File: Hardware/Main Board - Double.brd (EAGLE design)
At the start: 124.5 x 73.7 mm, 104 parts, among them J1 MICROMOD-2222-C, J10 MICRO-SD-PUSH-PUSH-EXT-PIN, J2 Vertical Qwiic Connector, J4 QWIIC_RIGHT_ANGLE, J5 CORTEX_JTAG_DEBUG_MINIMUM_PTH, J6 MICROMOD_CARRIER, J7 MICROMOD_CARRIER, Q1 3.1A/30V/105mΩ, U2 MCP73831, U5 AP7361C-33

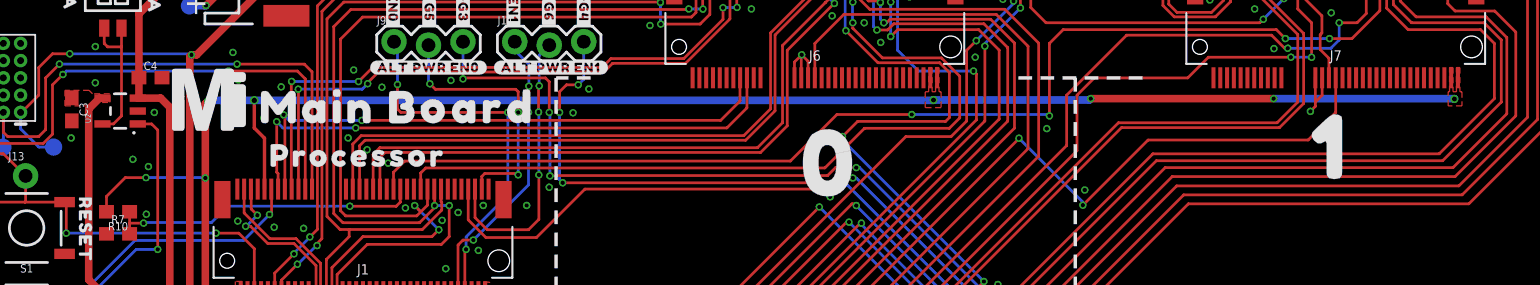
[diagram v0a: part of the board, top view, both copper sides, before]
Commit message: Changes power to Function Boards @ VCC to VCC rather than VIN
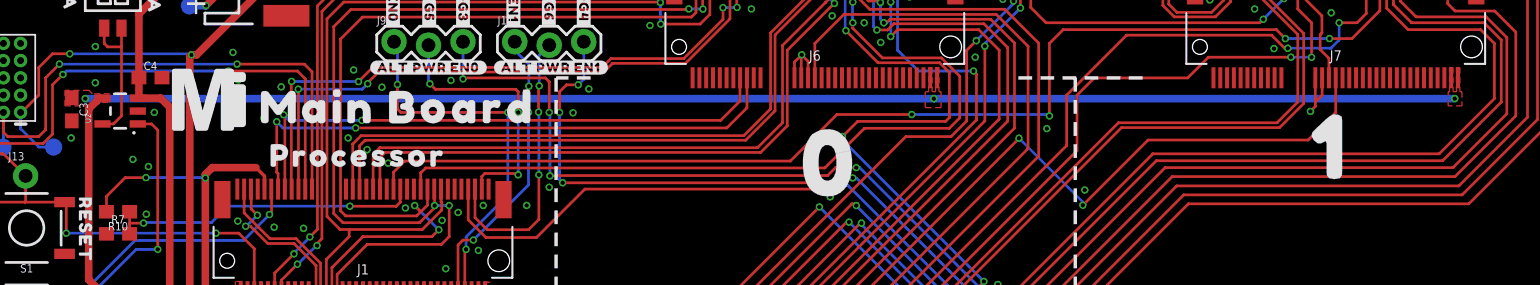
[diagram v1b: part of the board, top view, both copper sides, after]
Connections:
- net VCC: now also J6.72, J6.74, J7.72, J7.74
- net VIN: no longer J6.72, J6.74, J7.72, J7.74
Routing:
- net VCC: track 55.5 -> 156.4 mm, vias 2 -> 5
- net VIN: track 179.2 -> 80.7 mm, vias 9 -> 3
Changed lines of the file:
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@@
 <via x="37.4526" y="48.2628" extent="1-16" drill="0.3048"/>
 <via x="34.7856" y="50.4726" extent="1-16" drill="0.3048"/>
+<wire x1="21.206" y1="52.773" x2="19.706" y2="52.773" width="0" layer="19" extent="1-1"/>
+<wire x1="22.4158" y1="49.9646" x2="19.7358" y2="50.419" width="0" layer="19" extent="1-1"/>
 </signal>
 <signal name="V_BATT" class="1">
@@
 <wire x1="2.286" y1="29.972" x2="5.2324" y2="29.972" width="0.2032" layer="1"/>
 <wire x1="9.7743" y1="59.4716" x2="9.5606" y2="59.4716" width="0.5588" layer="1"/>
-<wire x1="9.5606" y1="59.4716" x2="8.763" y2="58.674" width="0.5588" layer="1"/>
+<wire x1="9.5606" y1="59.4716" x2="9.3345" y2="59.2455" width="0.5588" layer="1"/>
+<wire x1="9.3345" y1="59.2455" x2="8.763" y2="58.674" width="0.5588" layer="1"/>
 <wire x1="8.763" y1="46.101" x2="8.763" y2="58.674" width="0.5588" layer="1"/>
 <wire x1="15.113" y1="28.321" x2="14.7066" y2="27.9146" width="0.5588" layer="1"/>
@@
 <contactref element="Q1" pad="2"/>
 <contactref element="D5" pad="C"/>
+<contactref element="J6" pad="72"/>
+<contactref element="J6" pad="74"/>
+<contactref element="J7" pad="72"/>
+<contactref element="J7" pad="74"/>
+<polygon width="0.127" layer="1" thermals="no">
+<vertex x="70.612" y="61.722"/>
+<vertex x="70.866" y="61.722"/>
+<vertex x="70.866" y="59.944"/>
+<vertex x="71.12" y="59.944"/>
+<vertex x="71.12" y="61.722"/>
+<vertex x="71.374" y="61.722"/>
+<vertex x="71.374" y="59.944"/>
+<vertex x="71.5264" y="59.944"/>
+<vertex x="71.5264" y="58.7756"/>
+<vertex x="70.358" y="58.7756"/>
+<vertex x="70.358" y="59.944"/>
+<vertex x="70.612" y="59.944"/>
+</polygon>
+<polygon width="0.127" layer="1" thermals="no">
+<vertex x="108.966" y="61.722"/>
+<vertex x="109.22" y="61.722"/>
+<vertex x="109.22" y="59.944"/>
+<vertex x="109.474" y="59.944"/>
+<vertex x="109.474" y="61.722"/>
+<vertex x="109.728" y="61.722"/>
+<vertex x="109.728" y="59.944"/>
+<vertex x="109.8804" y="59.944"/>
+<vertex x="109.8804" y="58.9026"/>
+<vertex x="108.8644" y="58.9026"/>
+<vertex x="108.8644" y="59.944"/>
+<vertex x="108.966" y="59.944"/>
+</polygon>
+<via x="8.509" y="59.436" extent="1-16" drill="0.3048"/>
+<wire x1="8.509" y1="59.436" x2="70.993" y2="59.436" width="0.5588" layer="16"/>
+<via x="109.347" y="59.436" extent="1-16" drill="0.3048"/>
+<wire x1="70.993" y1="59.436" x2="109.347" y2="59.436" width="0.5588" layer="16"/>
+<via x="70.993" y="59.436" extent="1-16" drill="0.3048"/>
 </signal>
 <signal name="!CS1!-PROCESSOR">
@@
 <contactref element="R8" pad="2"/>
 <contactref element="D5" pad="A"/>
-<contactref element="J7" pad="72"/>
-<contactref element="J7" pad="74"/>
-<contactref element="J6" pad="72"/>
-<contactref element="J6" pad="74"/>
 <wire x1="13.1826" y1="15.748" x2="13.6652" y2="16.2306" width="0.5588" layer="1"/>
 <wire x1="13.6652" y1="16.2306" x2="13.6652" y2="16.9094" width="0.5588" layer="1"/>
 <wire x1="13.6652" y1="16.9094" x2="15.1314" y2="16.9094" width="0.5588" layer="1"/>
 <wire x1="15.1314" y1="16.9094" x2="17.3482" y2="19.1262" width="0.5588" layer="1"/>
-<via x="17.5514" y="59.2582" extent="1-16" drill="0.35"/>
-<wire x1="17.3482" y1="59.055" x2="17.3482" y2="53.594" width="0.5588" layer="1"/>
+<wire x1="17.3482" y1="53.594" x2="17.3482" y2="53.848" width="0.5588" layer="1"/>
 <wire x1="17.3482" y1="53.594" x2="17.3482" y2="19.1262" width="0.5588" layer="1"/>
-<wire x1="17.3482" y1="59.055" x2="17.5514" y2="59.2582" width="0.5588" layer="1"/>
-<wire x1="17.5514" y1="59.2582" x2="17.6022" y2="59.309" width="0.5588" layer="16"/>
-<polygon width="0.127" layer="1" thermals="no">
-<vertex x="108.966" y="61.722"/>
-<vertex x="109.22" y="61.722"/>
-<vertex x="109.22" y="59.944"/>
-<vertex x="109.474" y="59.944"/>
-<vertex x="109.474" y="61.722"/>
-<vertex x="109.728" y="61.722"/>
-<vertex x="109.728" y="59.944"/>
-<vertex x="109.8804" y="59.944"/>
-<vertex x="109.8804" y="58.9026"/>
-<vertex x="108.8644" y="58.9026"/>
-<vertex x="108.8644" y="59.944"/>
-<vertex x="108.966" y="59.944"/>
-</polygon>
-<polygon width="0.127" layer="1" thermals="no">
-<vertex x="70.612" y="61.722"/>
-<vertex x="70.866" y="61.722"/>
-<vertex x="70.866" y="59.944"/>
-<vertex x="71.12" y="59.944"/>
-<vertex x="71.12" y="61.722"/>
-<vertex x="71.374" y="61.722"/>
-<vertex x="71.374" y="59.944"/>
-<vertex x="71.5264" y="59.944"/>
-<vertex x="71.5264" y="58.7756"/>
-<vertex x="70.358" y="58.7756"/>
-<vertex x="70.358" y="59.944"/>
-<vertex x="70.612" y="59.944"/>
-</polygon>
-<wire x1="17.6022" y1="59.309" x2="20.955" y2="59.309" width="0.5588" layer="16"/>
-<wire x1="20.955" y1="59.309" x2="70.9422" y2="59.309" width="0.5588" layer="16"/>
-<wire x1="70.9422" y1="59.309" x2="70.9676" y2="59.3344" width="0.5588" layer="16"/>
-<via x="70.9676" y="59.3344" extent="1-16" drill="0.35"/>
-<wire x1="109.3343" y1="59.4233" x2="109.3216" y2="59.4106" width="0.5588" layer="16"/>
-<via x="109.3216" y="59.4106" extent="1-16" drill="0.35"/>
-<wire x1="70.9676" y1="59.3344" x2="82.4484" y2="59.3344" width="0.5588" layer="16"/>
-<wire x1="82.4484" y1="59.3344" x2="82.55" y2="59.436" width="0.5588" layer="16"/>
-<via x="82.55" y="59.436" extent="1-16" drill="0.3048"/>
-<wire x1="82.55" y1="59.436" x2="96.012" y2="59.436" width="0.5588" layer="1"/>
-<via x="96.012" y="59.436" extent="1-16" drill="0.3048"/>
-<wire x1="96.012" y1="59.436" x2="109.3216" y2="59.436" width="0.5588" layer="16"/>
-<wire x1="109.3216" y1="59.436" x2="109.3343" y2="59.4233" width="0.5588" layer="16"/>
 <wire x1="4.3688" y1="27.21055" x2="4.3688" y2="26.1112" width="0.2032" layer="1"/>
 <wire x1="10.072" y1="51.1048" x2="10.072" y2="52.236" width="0.2032" layer="1"/>
@@
 <wire x1="10.072" y1="52.236" x2="11.4554" y2="53.6194" width="0.2032" layer="1"/>
 <contactref element="J1" pad="9"/>
-<wire x1="20.955" y1="57.277" x2="20.955" y2="59.309" width="0.254" layer="1"/>
-<via x="20.955" y="59.309" extent="1-16" drill="0.381"/>
-<wire x1="21.706" y1="52.773" x2="21.706" y2="56.526" width="0.254" layer="1"/>
-<wire x1="21.706" y1="56.526" x2="20.955" y2="57.277" width="0.254" layer="1"/>
 <contactref element="BYP" pad="2"/>
 <contactref element="F2" pad="2"/>
@@
 <wire x1="7.747" y1="17.438" x2="8.851" y2="17.438" width="0.2032" layer="1"/>
 <wire x1="8.851" y1="17.438" x2="8.89" y2="17.399" width="0.2032" layer="1"/>
+<wire x1="17.8562" y1="54.356" x2="21.082" y2="54.356" width="0.5588" layer="1"/>
+<wire x1="17.3482" y1="53.848" x2="17.8562" y2="54.356" width="0.5588" layer="1"/>
+<wire x1="21.706" y1="52.773" x2="21.706" y2="53.732" width="0.254" layer="1"/>
+<wire x1="21.706" y1="53.732" x2="21.082" y2="54.356" width="0.254" layer="1"/>
 </signal>
 <signal name="SHLD">

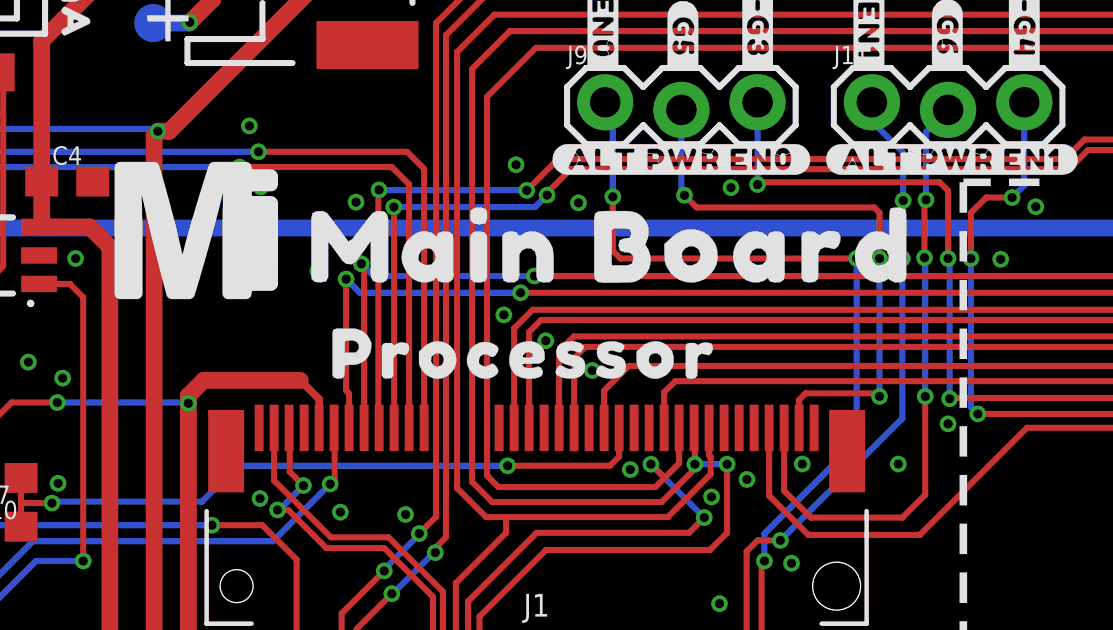
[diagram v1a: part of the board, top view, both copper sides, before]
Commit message: Adds two GND vias
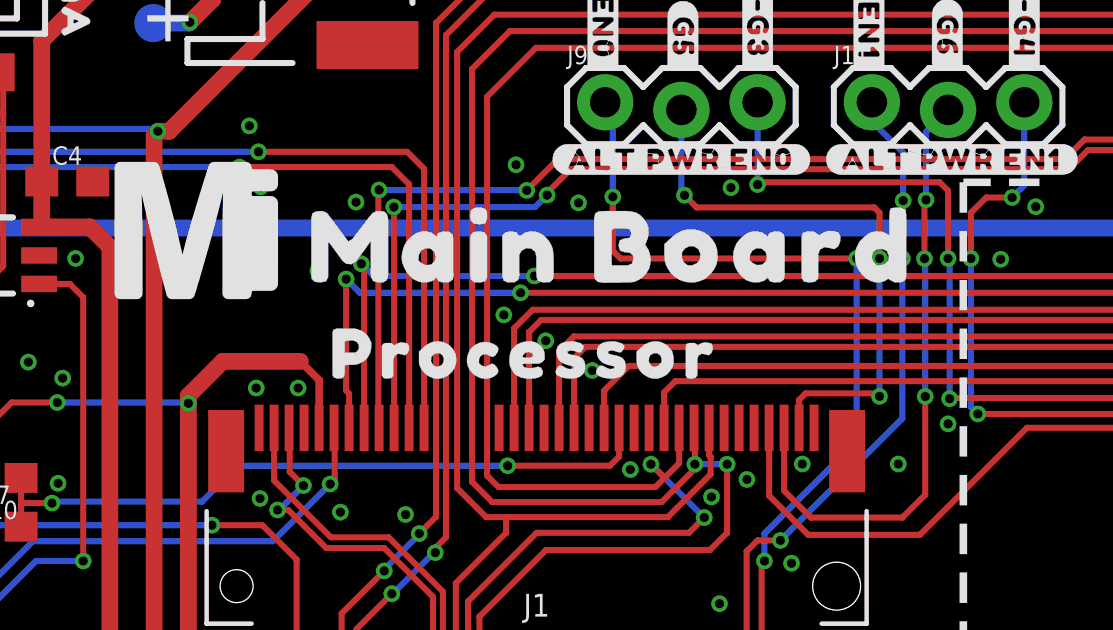
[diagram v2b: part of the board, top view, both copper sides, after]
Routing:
- net VIN: track 80.7 -> 81.6 mm
- net GND: vias 82 -> 84
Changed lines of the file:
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@@
 <via x="37.4526" y="48.2628" extent="1-16" drill="0.3048"/>
 <via x="34.7856" y="50.4726" extent="1-16" drill="0.3048"/>
-<wire x1="21.206" y1="52.773" x2="19.706" y2="52.773" width="0" layer="19" extent="1-1"/>
-<wire x1="22.4158" y1="49.9646" x2="19.7358" y2="50.419" width="0" layer="19" extent="1-1"/>
+<via x="19.6088" y="54.102" extent="1-16" drill="0.3048"/>
+<via x="21.0058" y="54.102" extent="1-16" drill="0.3048"/>
 </signal>
 <signal name="V_BATT" class="1">
@@
 <wire x1="7.747" y1="17.438" x2="8.851" y2="17.438" width="0.2032" layer="1"/>
 <wire x1="8.851" y1="17.438" x2="8.89" y2="17.399" width="0.2032" layer="1"/>
-<wire x1="17.8562" y1="54.356" x2="21.082" y2="54.356" width="0.5588" layer="1"/>
-<wire x1="17.3482" y1="53.848" x2="17.8562" y2="54.356" width="0.5588" layer="1"/>
-<wire x1="21.706" y1="52.773" x2="21.706" y2="53.732" width="0.254" layer="1"/>
-<wire x1="21.706" y1="53.732" x2="21.082" y2="54.356" width="0.254" layer="1"/>
+<wire x1="18.4912" y1="54.991" x2="21.082" y2="54.991" width="0.5588" layer="1"/>
+<wire x1="17.3482" y1="53.848" x2="18.4912" y2="54.991" width="0.5588" layer="1"/>
+<wire x1="21.706" y1="52.773" x2="21.706" y2="54.367" width="0.254" layer="1"/>
+<wire x1="21.706" y1="54.367" x2="21.082" y2="54.991" width="0.254" layer="1"/>
 </signal>
 <signal name="SHLD">
@@
 <contactref element="J1" pad="71"/>
 <via x="41.91" y="53.8226" extent="1-16" drill="0.3048"/>
-<wire x1="41.91" y1="53.8226" x2="41.91" y2="58.42" width="0.2032" layer="16"/>
-<wire x1="41.91" y1="58.42" x2="41.8846" y2="58.4454" width="0.2032" layer="16"/>
-<via x="41.8846" y="58.4454" extent="1-16" drill="0.3048"/>
+<wire x1="41.91" y1="53.8226" x2="41.91" y2="58.39" width="0.2032" layer="16"/>
+<wire x1="41.91" y1="58.39" x2="41.8846" y2="58.4154" width="0.2032" layer="16"/>
+<via x="41.8846" y="58.4154" extent="1-16" drill="0.3048"/>
 <wire x1="41.8846" y1="60.325" x2="41.9354" y2="60.3758" width="0.2032" layer="1"/>
-<wire x1="41.8846" y1="60.325" x2="41.8846" y2="58.4454" width="0.2032" layer="1"/>
+<wire x1="41.8846" y1="60.325" x2="41.8846" y2="58.4154" width="0.2032" layer="1"/>
 <via x="41.9354" y="60.3758" extent="1-16" drill="0.3048"/>
 <wire x1="41.9354" y1="60.3758" x2="41.9354" y2="62.6364" width="0.2032" layer="16"/>

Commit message: Rolls to v11
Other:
- board text added: "v11"
- board text removed: "v10"
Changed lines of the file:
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@@
 <wire x1="124.46" y1="73.66" x2="124.46" y2="0" width="0.2032" layer="20"/>
 <wire x1="0" y1="73.66" x2="0" y2="0" width="0.2032" layer="20"/>
-<text x="9.9568" y="1.4224" size="1.27" layer="16" font="vector" ratio="15" rot="MR0" align="center">v10</text>
+<text x="9.9568" y="1.4224" size="1.27" layer="16" font="vector" ratio="15" rot="MR0" align="center">v11</text>
 <text x="43.18" y="-25.654" size="1.778" layer="51" font="vector">Elias Santistevan</text>
 <text x="55.372" y="85.344" size="1.778" layer="47" font="vector" ratio="15">Units in Inches</text>

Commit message: Replaces schottky diode
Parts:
- D5: value 3A/10V/280mV -> 1A/23V/620mV
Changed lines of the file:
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@@
 <attribute name="VALUE" x="10.922" y="51.8668" size="0.6096" layer="27" font="vector" ratio="20" rot="R180" align="top-center"/>
 </element>
-<element name="D5" library="SparkFun-DiscreteSemi" package="SOD-323" value="3A/10V/280mV" x="13.6652" y="18.0594" smashed="yes" rot="R270">
+<element name="D5" library="SparkFun-DiscreteSemi" package="SOD-323" value="1A/23V/620mV" x="13.6652" y="18.0594" smashed="yes" rot="R270">
 <attribute name="NAME" x="14.4272" y="18.0594" size="0.6096" layer="25" font="vector" ratio="20" rot="R270" align="bottom-center"/>
-<attribute name="PROD_ID" value="DIO-14072" x="13.6652" y="18.0594" size="1.778" layer="27" font="vector" ratio="15" rot="R270" display="off"/>
-<attribute name="VALUE" x="12.9032" y="18.0594" size="0.6096" layer="27" font="vector" ratio="20" rot="R270" align="top-center"/>
+<attribute name="PROD_ID" value="DIO-11623" x="13.6652" y="18.0594" size="1.778" layer="27" font="vector" ratio="15" rot="R270" display="off"/>
+<attribute name="VALUE" value="1A/23V/620mV" x="12.9032" y="18.0594" size="0.6096" layer="27" font="vector" ratio="20" rot="R270" align="top-center"/>
 </element>
 <element name="J6" library="SparkFun-MicroMod-Function" package="M.2-CONNECTOR-E-FUNCTION-STANDARD" value="MICROMOD_CARRIER" x="62.23" y="63.246" smashed="yes" rot="R180">

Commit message: Updates Function board symbol, fixes some text explaining two pin jumper, corrects charging current.
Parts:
- 3V3_LED, 5V_LED: value (none) -> JUMPER-SMT_2_NC_TRACE_SILK
- VE: value (none) -> JUMPER-SMT_2_NO_SILK
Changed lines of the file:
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@@
 <attribute name="VALUE" x="9.8044" y="39.9796" size="0.6096" layer="27" font="vector" ratio="20" rot="R180" align="top-center"/>
 </element>
-<element name="VE" library="SparkFun-Jumpers" package="SMT-JUMPER_2_NO_SILK" package3d_urn="urn:adsk.eagle:package:39279/1" value="" x="9.6266" y="30.5054" smashed="yes" rot="MR270">
+<element name="VE" library="SparkFun-Jumpers" package="SMT-JUMPER_2_NO_SILK" package3d_urn="urn:adsk.eagle:package:39279/1" value="JUMPER-SMT_2_NO_SILK" x="9.6266" y="30.5054" smashed="yes" rot="MR270">
 <attribute name="NAME" x="8.4836" y="30.5054" size="0.6096" layer="26" font="vector" ratio="20" rot="MR270" align="bottom-center"/>
 <attribute name="VALUE" x="10.7696" y="30.5054" size="0.6096" layer="28" font="vector" ratio="20" rot="MR270" align="top-center"/>
 </element>
-<element name="3V3_LED" library="SparkFun-Jumpers" package="SMT-JUMPER_2_NC_TRACE_SILK" package3d_urn="urn:adsk.eagle:package:39281/1" value="" x="2.0828" y="32.3451" smashed="yes" rot="MR270">
+<element name="3V3_LED" library="SparkFun-Jumpers" package="SMT-JUMPER_2_NC_TRACE_SILK" package3d_urn="urn:adsk.eagle:package:39281/1" value="JUMPER-SMT_2_NC_TRACE_SILK" x="2.0828" y="32.3451" smashed="yes" rot="MR270">
 <attribute name="NAME" x="0.9398" y="32.3451" size="0.6096" layer="26" font="vector" ratio="20" rot="MR270" align="bottom-center"/>
 <attribute name="VALUE" x="3.2258" y="32.3451" size="0.6096" layer="28" font="vector" ratio="20" rot="MR270" align="top-center"/>
@@
 <attribute name="VALUE" x="25.019" y="18.3134" size="0.6096" layer="27" font="vector" ratio="20" rot="R90" align="top-center"/>
 </element>
-<element name="5V_LED" library="SparkFun-Jumpers" package="SMT-JUMPER_2_NC_TRACE_SILK" package3d_urn="urn:adsk.eagle:package:39281/1" value="" x="2.2098" y="27.93355" smashed="yes" rot="MR270">
+<element name="5V_LED" library="SparkFun-Jumpers" package="SMT-JUMPER_2_NC_TRACE_SILK" package3d_urn="urn:adsk.eagle:package:39281/1" value="JUMPER-SMT_2_NC_TRACE_SILK" x="2.2098" y="27.93355" smashed="yes" rot="MR270">
 <attribute name="NAME" x="1.0668" y="27.93355" size="0.6096" layer="26" font="vector" ratio="20" rot="MR270" align="bottom-center"/>
 <attribute name="VALUE" x="3.3528" y="27.93355" size="0.6096" layer="28" font="vector" ratio="20" rot="MR270" align="top-center"/>

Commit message: Updates the design to use the Micromod-function device in the official SFE Eagle Libs
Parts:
- J6, J7: value MICROMOD_CARRIER -> MICROMOD_FUNCTION_MAIN; device SparkFun-MicroMod-Function:M.2-CONNECTOR-E-FUNCTION-STANDARD -> SparkFun-MicroMod:M.2-CONNECTOR-E-FUNCTION-STANDARD
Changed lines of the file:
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@@
 <?xml version="1.0" encoding="utf-8"?>
 <!DOCTYPE eagle SYSTEM "eagle.dtd">
-<eagle version="9.6.2">
+<eagle version="9.5.1">
 <drawing>
 <settings>
@@
 <attribute name="VALUE" value="1A/23V/620mV" x="12.9032" y="18.0594" size="0.6096" layer="27" font="vector" ratio="20" rot="R270" align="top-center"/>
 </element>
-<element name="J6" library="SparkFun-MicroMod-Function" package="M.2-CONNECTOR-E-FUNCTION-STANDARD" value="MICROMOD_CARRIER" x="62.23" y="63.246" smashed="yes" rot="R180">
+<element name="J6" library="SparkFun-MicroMod" package="M.2-CONNECTOR-E-FUNCTION-STANDARD" value="MICROMOD_FUNCTION_MAIN" x="62.23" y="63.246" smashed="yes" rot="R180">
 <attribute name="NAME" x="62.23" y="62.611" size="0.762" layer="25" rot="R180" align="center"/>
 <attribute name="PROD_ID" value="CONN-14877" x="62.23" y="63.246" size="1.778" layer="27" rot="R180" display="off"/>
 <attribute name="VALUE" x="62.23" y="63.881" size="0.762" layer="27" rot="R180" align="center"/>
 </element>
-<element name="J7" library="SparkFun-MicroMod-Function" package="M.2-CONNECTOR-E-FUNCTION-STANDARD" value="MICROMOD_CARRIER" x="100.584" y="63.246" smashed="yes" rot="R180">
+<element name="J7" library="SparkFun-MicroMod" package="M.2-CONNECTOR-E-FUNCTION-STANDARD" value="MICROMOD_FUNCTION_MAIN" x="100.584" y="63.246" smashed="yes" rot="R180">
 <attribute name="NAME" x="100.584" y="62.611" size="0.762" layer="25" rot="R180" align="center"/>
 <attribute name="PROD_ID" value="CONN-14877" x="100.584" y="63.246" size="1.778" layer="27" rot="R180" display="off"/>
